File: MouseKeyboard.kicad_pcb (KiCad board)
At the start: 2 copper layers, 83.8 x 68.6 mm, 20 parts, among them IC1 ATMEGA328P-P, J1 USB, SW1 SW_PUSH, SW2 SW_PUSH, SW3 SW_PUSH, SW4 SW_PUSH, SW5 SW_PUSH, SW6 SW_PUSH, SW7 SW_PUSH, SW8 SPST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

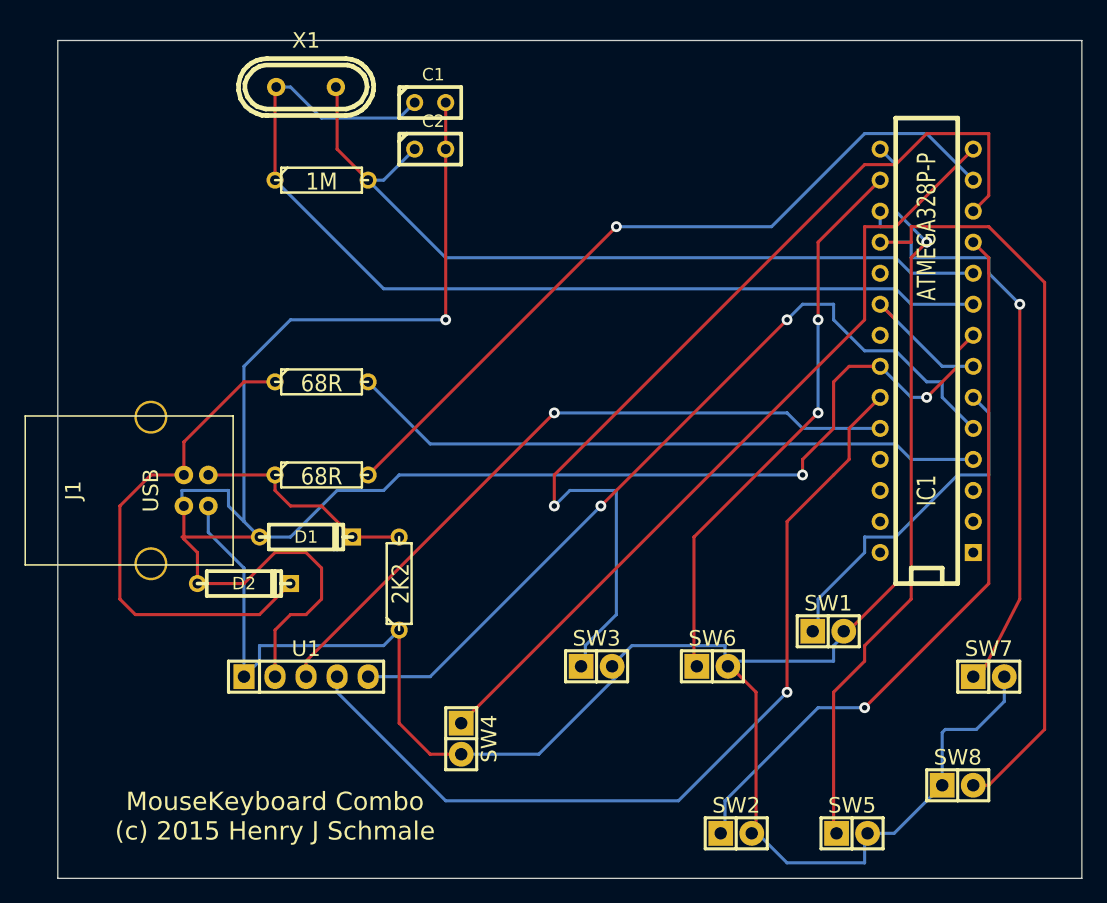
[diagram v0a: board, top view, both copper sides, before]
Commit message: Shrunk the PCB a bit
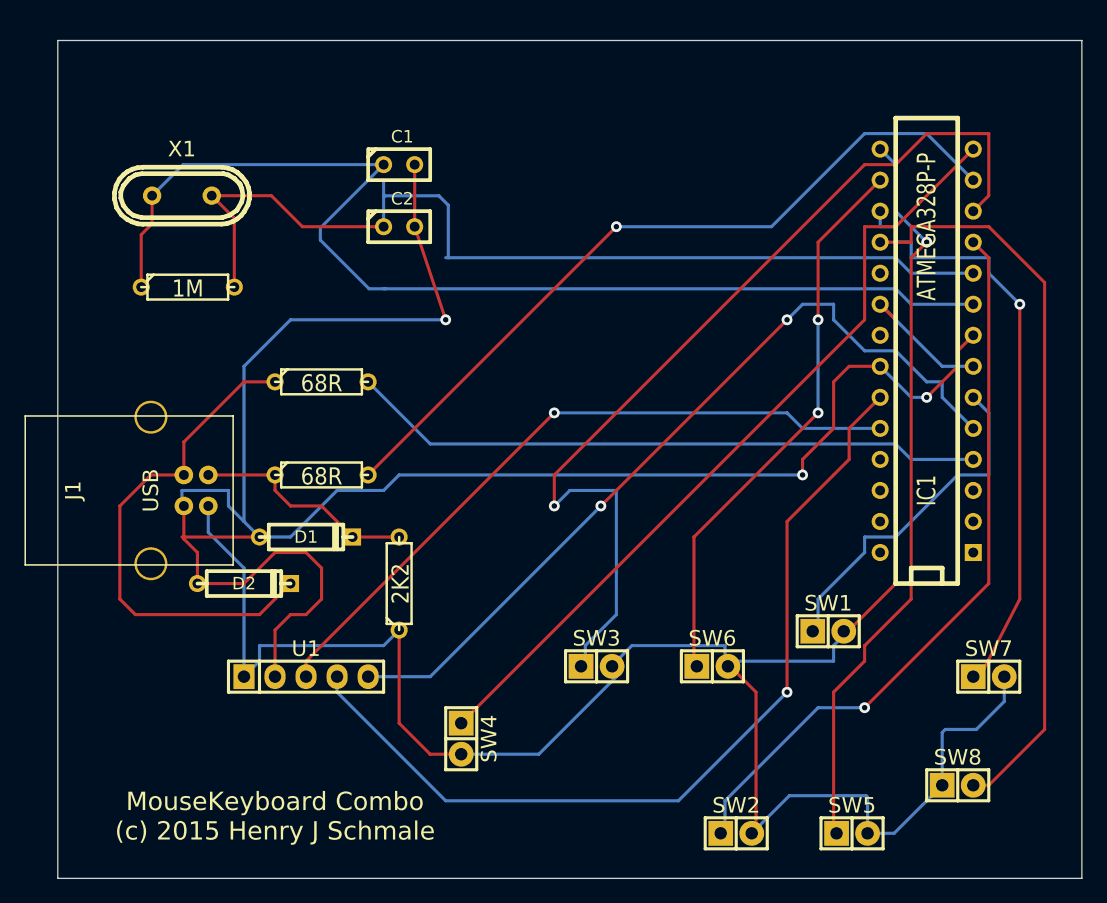
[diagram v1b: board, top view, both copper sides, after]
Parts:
- moved R4 14.0 mm to (109.7, 86.2)
- moved X1 13.5 mm to (109.2, 78.7)
- moved C2 6.84 mm to (127.0, 81.3)
- moved C1 5.68 mm to (127.0, 76.2)
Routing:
- net XTAL2: track 66.4 -> 81.0 mm
- net XTAL1: track 82.1 -> 92.1 mm
- net GND: track 165.9 -> 161.2 mm
- net +5V: track 175.8 -> 177.1 mm

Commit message: Copper Infill
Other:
- board size 83.8 x 68.6 mm -> 79.4 x 62.2 mm

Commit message: Finished Layout, now if only it would print
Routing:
- net GND: track 161.2 -> 158.2 mm
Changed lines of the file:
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@@
     (area 96.075499 65.989999 182.930001 134.670001)
     (thickness 1.6)
-    (drawings 7)
+    (drawings 8)
     (tracks 255)
     (zones 0)
@@
       (net 3 XTAL2))
   )
+  (dimension 79.375 (width 0.3) (layer Dwgs.User)
+    (gr_text "79.375 mm" (at 141.2875 141.685) (layer Dwgs.User)
+      (effects (font (size 1.5 1.5) (thickness 0.3)))
+    )
+    (feature1 (pts (xy 180.975 133.35) (xy 180.975 143.035)))
+    (feature2 (pts (xy 101.6 133.35) (xy 101.6 143.035)))
+    (crossbar (pts (xy 101.6 140.335) (xy 180.975 140.335)))
+    (arrow1a (pts (xy 180.975 140.335) (xy 179.848496 140.921421)))
+    (arrow1b (pts (xy 180.975 140.335) (xy 179.848496 139.748579)))
+    (arrow2a (pts (xy 101.6 140.335) (xy 102.726504 140.921421)))
+    (arrow2b (pts (xy 101.6 140.335) (xy 102.726504 139.748579)))
+  )
   (dimension 62.23 (width 0.3) (layer Dwgs.User)
     (gr_text "62.230 mm" (at 188.675 102.235 90) (layer Dwgs.User)
@@
   (segment (start 128.27 81.28) (end 128.27 76.2) (width 0.254) (layer F.Cu) (net 2) (status 20))
   (segment (start 114.3 92.71) (end 118.11 88.9) (width 0.254) (layer B.Cu) (net 2))
-  (segment (start 118.11 88.9) (end 130.81 88.9) (width 0.254) (layer B.Cu) (net 2))
-  (via (at 130.81 88.9) (size 0.889) (layers F.Cu B.Cu) (net 2))
-  (segment (start 130.81 88.9) (end 128.27 81.28) (width 0.254) (layer F.Cu) (net 2) (status 20))
+  (segment (start 118.11 88.9) (end 128.27 88.9) (width 0.254) (layer B.Cu) (net 2))
+  (via (at 128.27 88.9) (size 0.889) (layers F.Cu B.Cu) (net 2))
+  (segment (start 128.27 88.9) (end 128.27 81.28) (width 0.254) (layer F.Cu) (net 2) (status 800020))
   (segment (start 114.3 105.41) (end 114.3 92.71) (width 0.254) (layer B.Cu) (net 2))
   (segment (start 115.57 106.68) (end 109.22 106.68) (width 0.254) (layer F.Cu) (net 2))
